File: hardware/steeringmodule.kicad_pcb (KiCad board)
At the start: 2 copper layers, 144 x 56.1 mm, 74 parts, among them J101 Conn_01x02, J102 PotConnector, J103 Conn_01x02, U201 MCP2561-E/SN, U202 MCP2515-I/SO, U301 LM7805_TO220, U401 ATMEGA328P-PU, U601 BTS7960B, U602 BTS7960B, Y401 16MHz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

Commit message: hardware: added 3D IMG archives and schematic PDF
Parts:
- D402, D403, R404, R405: moved to F.Cu
- J101, J103: footprint Connector_Phoenix_MSTB:PhoenixContact_MSTBA_2,5_2-G_1x02_P5.00mm_Horizontal -> TerminalBlock_Phoenix:TerminalBlock_Phoenix_MKDS-1,5-2-5.08_1x02_P5.08mm_Horizontal
- moved D402 24.9 mm to (114.0, 87.8), turned to 90 degrees
- moved R404 24.4 mm to (116.5, 87.8)
- moved D403 20.0 mm to (114.0, 92.8)
- moved R405 20.0 mm to (116.5, 92.8)
- moved J103 5.97 mm to (196.5, 101.8)
- moved J101 4.15 mm to (196.5, 86.7)
- moved H107 1.65 mm to (173.2, 79.4)
- moved H105 1.65 mm to (196.9, 68.6)
- moved H101 1.60 mm to (70.8, 68.6)
- moved H103 1.60 mm to (111.2, 68.6)
- moved H108 1.53 mm to (173.2, 108.7)
- moved RINH2 0.64 mm to (166.5, 101.7)
- moved RSR603 0.64 mm to (166.5, 103.9)
- moved CBTS2 0.41 mm to (166.5, 95.6)
- moved RSR2 0.38 mm to (166.5, 99.6)
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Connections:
- J101 pad 1: GNDPWR -> /HBRIDGE/VS1
- J101 pad 2: /HBRIDGE/VS1 -> GNDPWR
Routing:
- net /MCU/LED1: track 20.9 -> 7.65 mm, vias 2 -> 0
- net /MCU/LED2: track 18.5 -> 29.3 mm
- net /HBRIDGE/INPUT2: track 64.7 -> 57.2 mm, vias 2 -> 1
- net +5V: track 201.6 -> 197.3 mm
- net GND: track 32.7 -> 29.6 mm
- net GNDPWR: track 21.7 -> 20.3 mm
- net /HBRIDGE/INPUT1: track 54.5 -> 55.4 mm
- net Net-(RSR603-Pad2): track 5.47 -> 4.83 mm
- net Net-(RINH2-Pad2): track 5.10 -> 4.46 mm
- net Net-(D402-Pad2): track 1.91 -> 2.42 mm
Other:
- board size 144 x 56.1 mm -> 144 x 58.7 mm
- board text added: "MOTOR"
- board text removed: "+ MOTOR -"

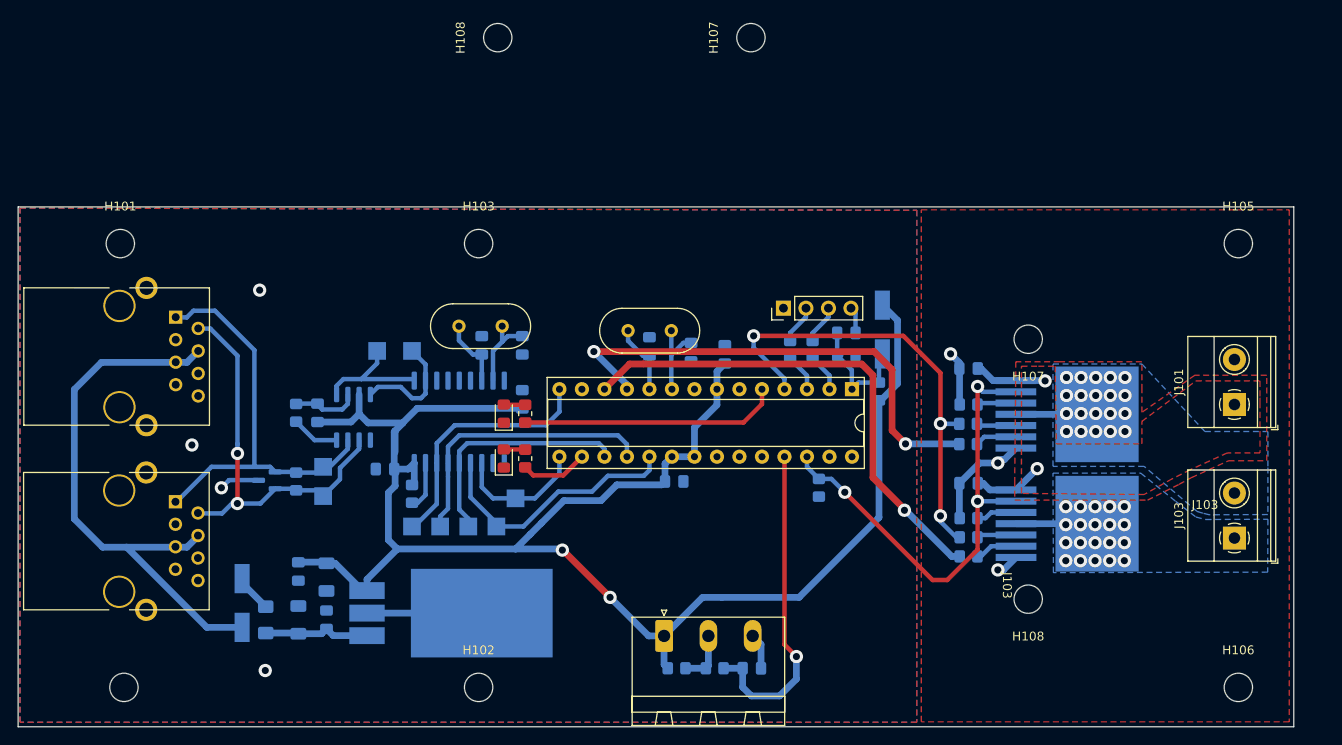
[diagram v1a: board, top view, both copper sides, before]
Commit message: Added analog stage for Vbat measurement, and it's simulation
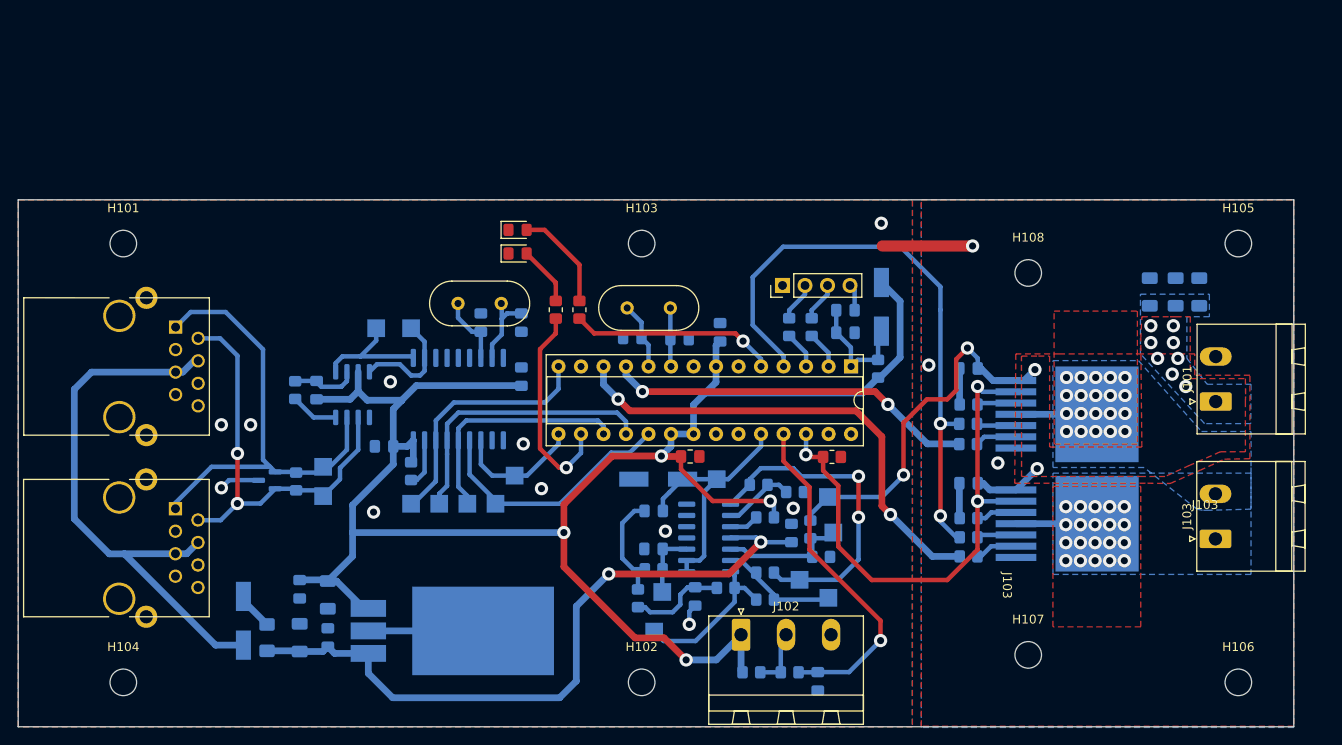
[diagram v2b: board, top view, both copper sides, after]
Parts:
- removed the H107 at (173.2, 79.4)
- removed the H108 at (173.2, 108.7)
- added C601: 1uF, Capacitor_SMD:C_1206_3216Metric_Pad1.33x1.80mm_HandSolder, B.Cu at (186.9, 74.0)
- added C602: 1uF, Capacitor_SMD:C_1206_3216Metric_Pad1.33x1.80mm_HandSolder, B.Cu at (189.9, 74.0)
- added C603: 1uF, Capacitor_SMD:C_1206_3216Metric_Pad1.33x1.80mm_HandSolder, B.Cu at (192.5, 74.0)
- added C701: 100n, Capacitor_SMD:C_0805_2012Metric_Pad1.18x1.45mm_HandSolder, B.Cu at (135.6, 108.4)
- added C702: 100n, Capacitor_SMD:C_0805_2012Metric_Pad1.18x1.45mm_HandSolder, B.Cu at (131.0, 98.8)
- added C703: 100n, Capacitor_SMD:C_0805_2012Metric_Pad1.18x1.45mm_HandSolder, B.Cu at (130.9, 103.0)
- added C704: 100n, Capacitor_SMD:C_0805_2012Metric_Pad1.18x1.45mm_HandSolder, B.Cu at (146.5, 101.2)
- added D701: 4V7, Diode_SMD:D_MiniMELF_Handsoldering, B.Cu at (131.5, 95.2)
- added R701: 10k, Resistor_SMD:R_0805_2012Metric_Pad1.20x1.40mm_HandSolder, B.Cu at (143.5, 99.5)
- added R702: 10k, Resistor_SMD:R_0805_2012Metric_Pad1.20x1.40mm_HandSolder, B.Cu at (143.5, 105.7)
- added R703: 10k, Resistor_SMD:R_0805_2012Metric_Pad1.20x1.40mm_HandSolder, B.Cu at (148.6, 100.8)
- added R704: 10k, Resistor_SMD:R_0805_2012Metric_Pad1.20x1.40mm_HandSolder, B.Cu at (146.9, 96.6)
- added R705: 11k, Resistor_SMD:R_0805_2012Metric_Pad1.20x1.40mm_HandSolder, B.Cu at (142.8, 95.8)
- added R706: 12k, Resistor_SMD:R_0805_2012Metric_Pad1.20x1.40mm_HandSolder, B.Cu at (143.5, 108.8)
- added R707: 12k, Resistor_SMD:R_0805_2012Metric_Pad1.20x1.40mm_HandSolder, B.Cu at (149.9, 103.9)
- added R708: 1k, Resistor_SMD:R_0805_2012Metric_Pad1.20x1.40mm_HandSolder, B.Cu at (139.1, 107.4)
- added R709: 1k, Resistor_SMD:R_0805_2012Metric_Pad1.20x1.40mm_HandSolder, B.Cu at (129.2, 108.6)
- added R710: 1k, Resistor_SMD:R_0805_2012Metric_Pad1.20x1.40mm_HandSolder, B.Cu at (131.0, 105.3)
- added TP702: VBAT, TestPoint:TestPoint_Pad_2.0x2.0mm, B.Cu at (150.6, 97.2)
- added TP703: op_a_in-, TestPoint:TestPoint_Pad_2.0x2.0mm, B.Cu at (150.7, 108.6)
- added TP704: op_a_in+, TestPoint:TestPoint_Pad_2.0x2.0mm, B.Cu at (151.2, 101.2)
- added TP705: Vref, TestPoint:TestPoint_Pad_2.0x2.0mm, B.Cu at (147.4, 106.5)
- added TP706: op_a_out, TestPoint:TestPoint_Pad_2.0x2.0mm, B.Cu at (131.0, 112.4)
- added TP707: op_b_in+, TestPoint:TestPoint_Pad_2.0x2.0mm, B.Cu at (131.9, 107.9)
- added TP708: op_b_out, TestPoint:TestPoint_Pad_2.0x2.0mm, B.Cu at (138.1, 95.2)
- added U701: LM324, Package_SO:SOIC-14_3.9x8.7mm_P1.27mm, B.Cu at (137.2, 101.8)
- C402, RIS1: moved to F.Cu
- H101, H102, H103, H104, H105, H106, H107, H108: footprint MountingHole:MountingHole_3.2mm_M3 -> MountingHole:MountingHole_3mm
- J101, J103: footprint TerminalBlock_Phoenix:TerminalBlock_Phoenix_MKDS-1,5-2-5.08_1x02_P5.08mm_Horizontal -> Connector_Phoenix_MSTB:PhoenixContact_MSTBA_2,5_2-G-5,08_1x02_P5.08mm_Horizontal
- J102: footprint Connector_Phoenix_MSTB:PhoenixContact_MSTBA_2,5_3-G_1x03_P5.00mm_Horizontal -> Connector_Phoenix_MSTB:PhoenixContact_MSTBA_2,5_3-G-5,08_1x03_P5.08mm_Horizontal
- moved H107 76.4 mm to (173.2, 115.0), turned to 0 degrees
- moved H108 65.5 mm to (173.2, 71.9), turned to 0 degrees
- moved D403 23.2 mm to (115.6, 69.7), turned to 0 degrees
- moved D402 20.8 mm to (115.6, 67.0), turned to 0 degrees
- moved H102 18.4 mm to (129.6, 118.1)
- moved H103 18.4 mm to (129.6, 68.6)
- moved R405 17.1 mm to (119.9, 76.0)
- moved R404 13.2 mm to (122.6, 76.0)
- moved J102 8.69 mm to (140.8, 112.7)
- moved R101 8.47 mm to (146.3, 117.0)
- moved R102 8.45 mm to (142.0, 117.0)
- moved C102 7.59 mm to (149.5, 118.0), turned to -90 degrees
- moved RIS1 3.78 mm to (151.1, 92.7), turned to 0 degrees
- moved C402 3.35 mm to (135.1, 92.6)
- moved C405 2.57 mm to (152.6, 76.1)
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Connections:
- net /POWER SUPPLY/+18V_OUT renamed /+18V
- CBTS1 pad 2: GNDPWR -> GND
- CBTS2 pad 2: GNDPWR -> GND
- J101 pad 2: GNDPWR -> GND
- J201 pad 9: (no net) -> GND
- J202 pad 9: (no net) -> GND
- RSR1 pad 2: GNDPWR -> GND
- RSR2 pad 2: GNDPWR -> GND
- U401 pad 24: unconnected-(U401-Pad24) -> /MCU/VBAT
- U601 pad 1: GNDPWR -> GND
- U602 pad 1: GNDPWR -> GND
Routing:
- net /+18V: track 12.1 -> 78.9 mm, vias 0 -> 2
- net /analog/Vref: track 0.00 -> 37.1 mm, vias 0 -> 2
- net /HBRIDGE/VS1: track 16.2 -> 50.1 mm, vias 2 -> 12
- net /MCU/VBAT: track 0.00 -> 29.0 mm
- net GNDPWR: track 20.3 -> 0.00 mm, vias 3 -> 0
- net Net-(R706-Pad1): track 0.00 -> 17.9 mm
- net /MCU/LED1: track 7.65 -> 23.7 mm, vias 0 -> 1
- net GND: track 29.6 -> 45.6 mm, vias 4 -> 14
- net /HBRIDGE/INH: track 52.0 -> 67.5 mm, vias 3 -> 2
- net Net-(R703-Pad1): track 0.00 -> 13.7 mm
- net Net-(R702-Pad1): track 0.00 -> 13.6 mm
- net /HBRIDGE/INPUT1: track 55.4 -> 41.8 mm
- net Net-(C702-Pad1): track 0.00 -> 12.7 mm
- net Net-(C701-Pad1): track 0.00 -> 11.0 mm
- net Net-(D402-Pad2): track 2.42 -> 11.7 mm
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- added copper zone on F.Cu, net /HBRIDGE/OUT1
- added copper zone on F.Cu, net /HBRIDGE/OUT2
- added copper zone on B.Cu, net /HBRIDGE/VS1
- removed copper zone on F.Cu, net GNDPWR
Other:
- board size 144 x 58.7 mm -> 144 x 59.5 mm
- board text removed: "6cm"

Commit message: Adjusted analog, now using INA826. Simulations updated.
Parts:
- removed R706, R707: 12k, Resistor_SMD:R_0805_2012Metric_Pad1.20x1.40mm_HandSolder
- removed R708, R709, R710: 1k, Resistor_SMD:R_0805_2012Metric_Pad1.20x1.40mm_HandSolder
- removed TP703: op_a_in-, TestPoint:TestPoint_Pad_2.0x2.0mm
- removed TP704: op_a_in+, TestPoint:TestPoint_Pad_2.0x2.0mm
- removed TP705: Vref, TestPoint:TestPoint_Pad_2.0x2.0mm
- removed TP706: op_a_out, TestPoint:TestPoint_Pad_2.0x2.0mm
- removed TP707: op_b_in+, TestPoint:TestPoint_Pad_2.0x2.0mm
- C701, C702: value 100n -> 1n
- C703: value 100n -> 1uF; footprint Capacitor_SMD:C_0805_2012Metric_Pad1.18x1.45mm_HandSolder -> Capacitor_SMD:C_1206_3216Metric_Pad1.33x1.80mm_HandSolder
- R701, R702: value 10k -> 22k
- R703, R704: value 10k -> 8k2
- R705: value 11k -> 100
- TP708: value op_b_out -> out1
- U701: value LM324 -> INA826_D_8; footprint Package_SO:SOIC-14_3.9x8.7mm_P1.27mm -> Package_SO:SOIC-8_3.9x4.9mm_P1.27mm
- moved C701 16.5 mm to (147.8, 97.3), turned to 180 degrees
- moved C702 15.4 mm to (144.8, 105.5), turned to 180 degrees
- moved R704 11.5 mm to (144.9, 107.9)
- moved D701 9.92 mm to (137.5, 103.1), turned to -90 degrees
- moved C703 9.48 mm to (135.2, 94.6)
- moved R705 6.56 mm to (136.4, 97.2), turned to 180 degrees
- moved R702 6.23 mm to (149.7, 104.6), turned to -90 degrees
- moved TP708 6.22 mm to (134.3, 100.1)
- moved R703 5.99 mm to (147.9, 94.9), turned to 180 degrees
- moved U701 5.87 mm to (143.0, 101.2)
- moved C704 5.46 mm to (142.7, 97.3), turned to 0 degrees
- moved R701 4.59 mm to (143.6, 94.9)
- moved TP702 3.71 mm to (149.8, 100.8)
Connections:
- C701 pad 1: Net-(C701-Pad1) -> GND
- C701 pad 2: GND -> Net-(C701-Pad2)
- C702 pad 2: /MCU/VBAT -> GND
- C703 pad 1: Net-(C703-Pad1) -> /MCU/VBAT
- D701 pad 1: /MCU/VBAT -> Net-(D701-Pad1)
- R701 pad 1: Net-(R701-Pad1) -> GND
- R701 pad 2: +5V -> Net-(C701-Pad2)
- R702 pad 1: Net-(R702-Pad1) -> /HBRIDGE/VS1
- R702 pad 2: /analog/Vref -> Net-(C702-Pad1)
- R703 pad 1: Net-(R703-Pad1) -> GND
- R703 pad 2: /HBRIDGE/VS1 -> Net-(C701-Pad2)
- R704 pad 1: GND -> Net-(C702-Pad1)
- R704 pad 2: Net-(R704-Pad2) -> GND
- R705 pad 1: /analog/Vref -> Net-(D701-Pad1)
- R705 pad 2: Net-(R704-Pad2) -> /MCU/VBAT
- TP708 pad 1: /MCU/VBAT -> Net-(D701-Pad1)
- U701 pad 1: /analog/Vref -> Net-(C701-Pad2)
- U701 pad 2: Net-(R704-Pad2) -> unconnected-(U701-Pad2)
- U701 pad 3: Net-(R701-Pad1) -> unconnected-(U701-Pad3)
- U701 pad 4: /+18V -> Net-(C702-Pad1)
- U701 pad 5: Net-(R703-Pad1) -> GND
- U701 pad 6: Net-(R702-Pad1) -> GND
- U701 pad 7: Net-(R706-Pad1) -> Net-(D701-Pad1)
- U701 pad 8: /MCU/VBAT -> /+18V
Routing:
- net /analog/Vref: track 37.1 -> 0.00 mm, vias 2 -> 0
- net Net-(R706-Pad1): track 17.9 -> 0.00 mm
- net /MCU/VBAT: track 29.0 -> 11.4 mm
- net +5V: track 206.4 -> 191.4 mm, vias 4 -> 3
- net Net-(R703-Pad1): track 13.7 -> 0.00 mm
- net Net-(R702-Pad1): track 13.6 -> 0.00 mm
- net Net-(C701-Pad1): track 11.0 -> 0.00 mm
- net Net-(D701-Pad1): track 0.00 -> 9.53 mm
- net Net-(R704-Pad2): track 8.17 -> 0.00 mm
- net Net-(C703-Pad1): track 7.60 -> 0.00 mm
- net Net-(C701-Pad2): track 0.00 -> 7.29 mm
- net Net-(C702-Pad1): track 12.7 -> 8.76 mm
- net Net-(R701-Pad1): track 3.33 -> 0.00 mm
- net GND: track 45.6 -> 43.0 mm, vias 14 -> 11
- net /HBRIDGE/IS: track 61.3 -> 62.9 mm, vias 3 -> 5
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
